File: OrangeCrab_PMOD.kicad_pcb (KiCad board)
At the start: 2 copper layers, 1 part

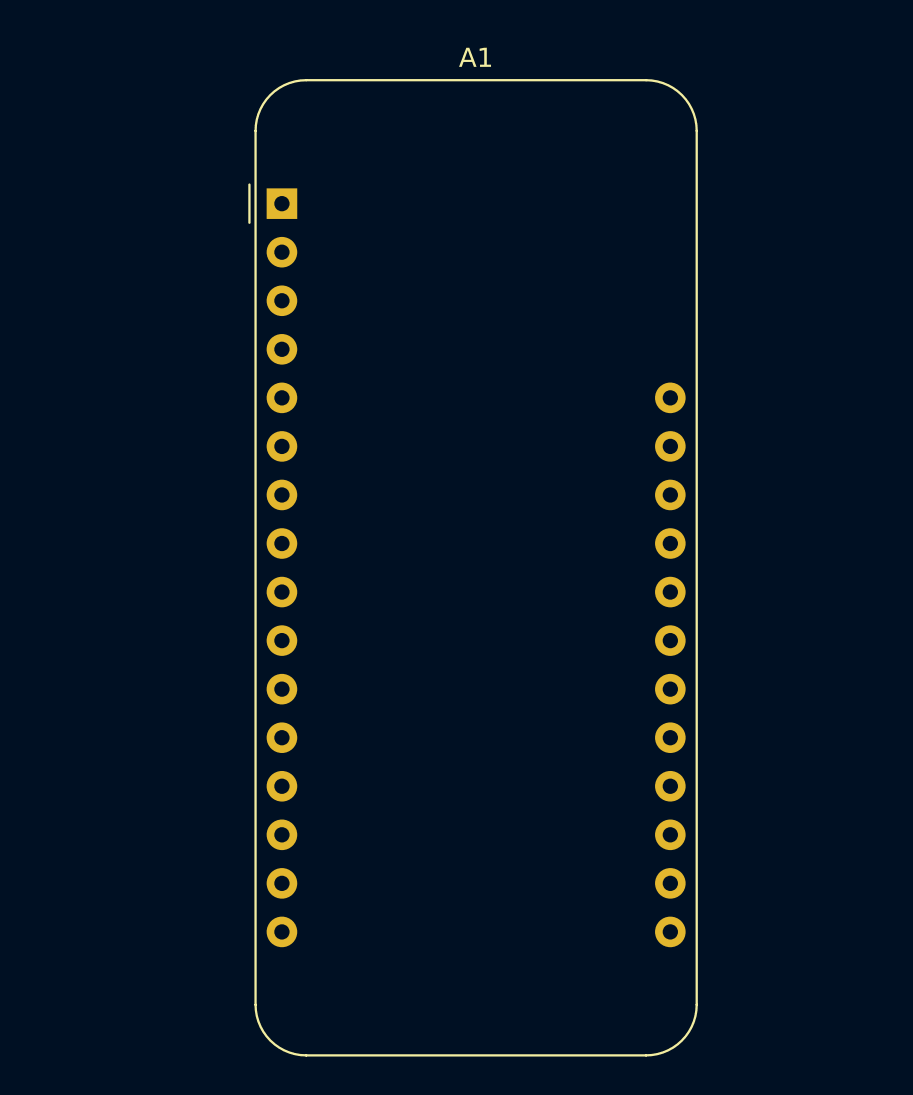
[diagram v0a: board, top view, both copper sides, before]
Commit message: started layout and connectors to Orange Crab
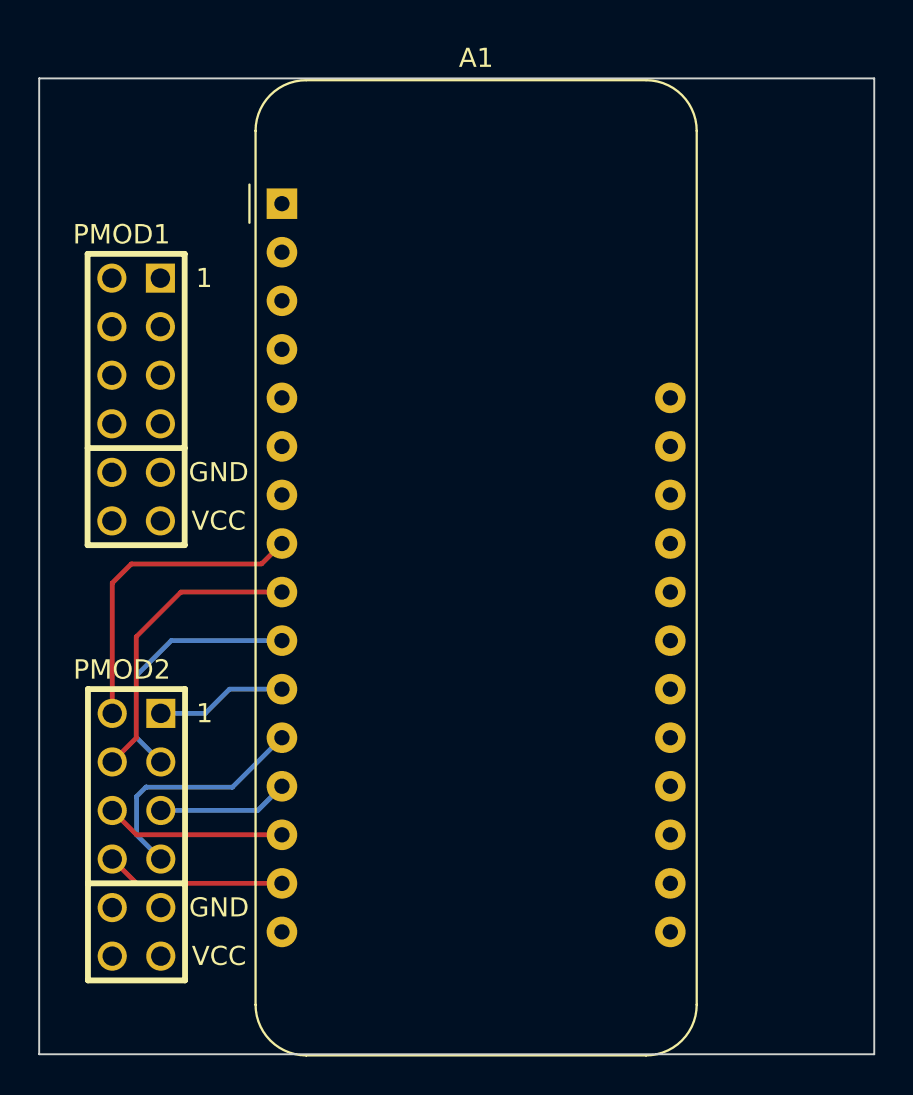
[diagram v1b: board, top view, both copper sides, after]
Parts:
- added PMOD1: PMOD-Device-x2-Type-XHS, pmod-conn_6x2:pmod_pin_array_6x2, F.Cu at (94.5, 91.7)
- added PMOD2: PMOD-Device-x2-Type-XHS, pmod-conn_6x2:pmod_pin_array_6x2, F.Cu at (94.5, 114.5)
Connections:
- A1 pad 2: unconnected-(A1-3V3-Pad2) -> /3V3
- A1 pad 21: /PT67A -> /PT67B
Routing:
- net /PR26A: track 0.00 -> 16.6 mm
- net /PR26B: track 0.00 -> 15.7 mm
- net /PB13B: track 0.00 -> 13.4 mm
- net /PB4B: track 0.00 -> 12.7 mm
- net /PB6B: track 0.00 -> 9.41 mm
- net /PB6A: track 0.00 -> 9.41 mm
- net /PB4A: track 0.00 -> 6.86 mm
- net /PB13A: track 0.00 -> 6.86 mm
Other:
- board outline added: 43.7 x 51.1 mm
